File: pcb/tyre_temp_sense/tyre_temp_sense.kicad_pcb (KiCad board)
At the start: 2 copper layers, 75 x 41.5 mm, 38 parts, among them J1 POWER & CAN, J2 MUX Port 0, J3 MUX Port 1, J4 MUX Port 2, J5 MUX Port 3, J6 Conn_01x02, J7 A, J8 GND, J9 GND, U1 TCA9548APWR, U2 MCP2515-I/ST, U3 MCP2551-I-SN, Y1 8 mhz

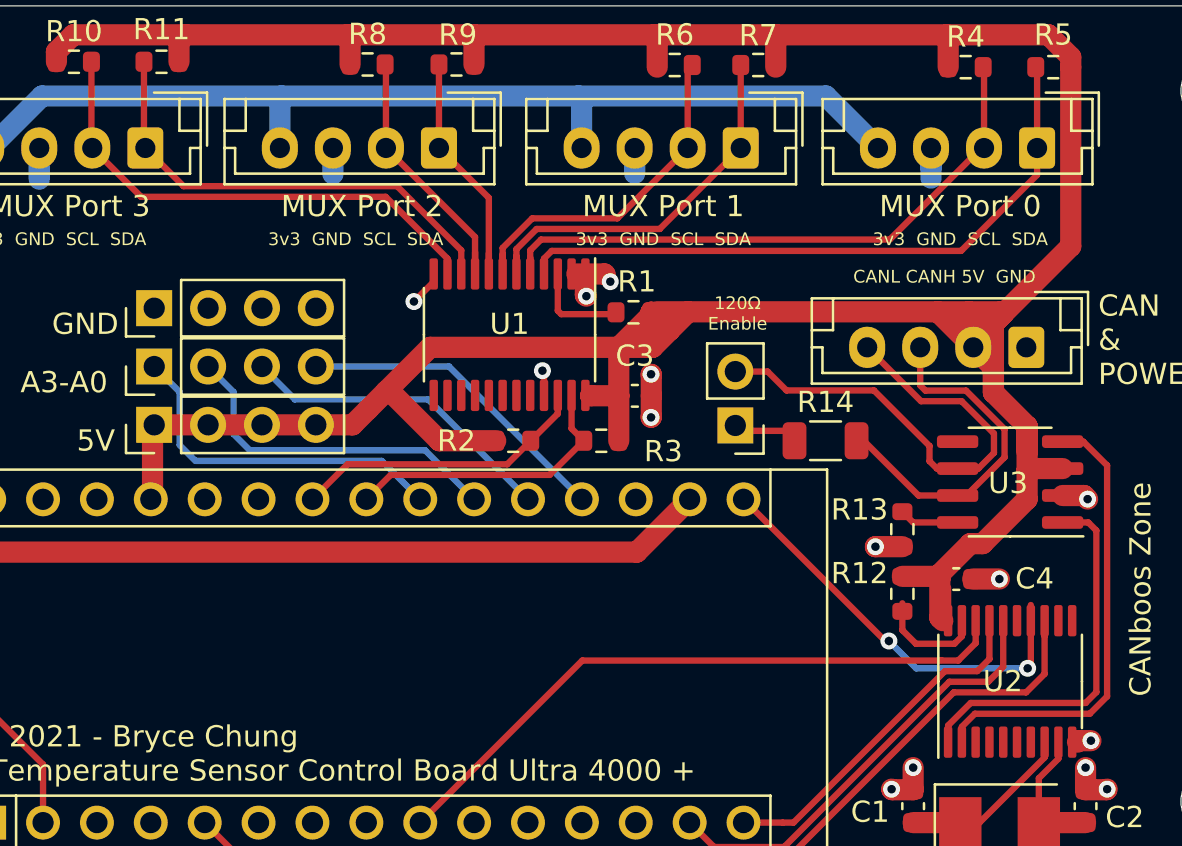
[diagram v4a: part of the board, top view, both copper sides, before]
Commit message: Gerbers, drill, BOM and part pos added
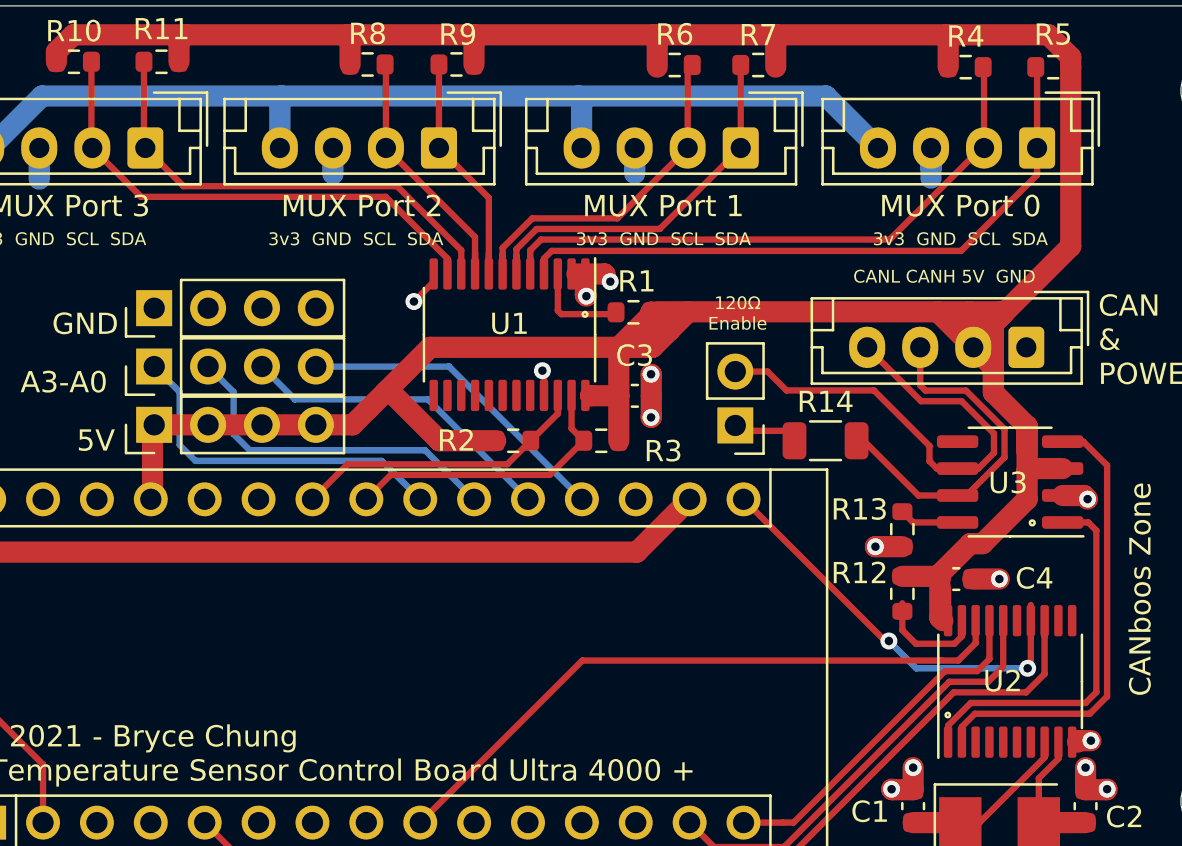
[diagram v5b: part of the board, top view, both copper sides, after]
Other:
- board text added: "The seatbelt sign has been switched on. Please refrain from walking about the I²C bus while the sign is on."
